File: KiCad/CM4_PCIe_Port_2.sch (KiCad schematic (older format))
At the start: 1 part, among them J14 10018783-10113TLF

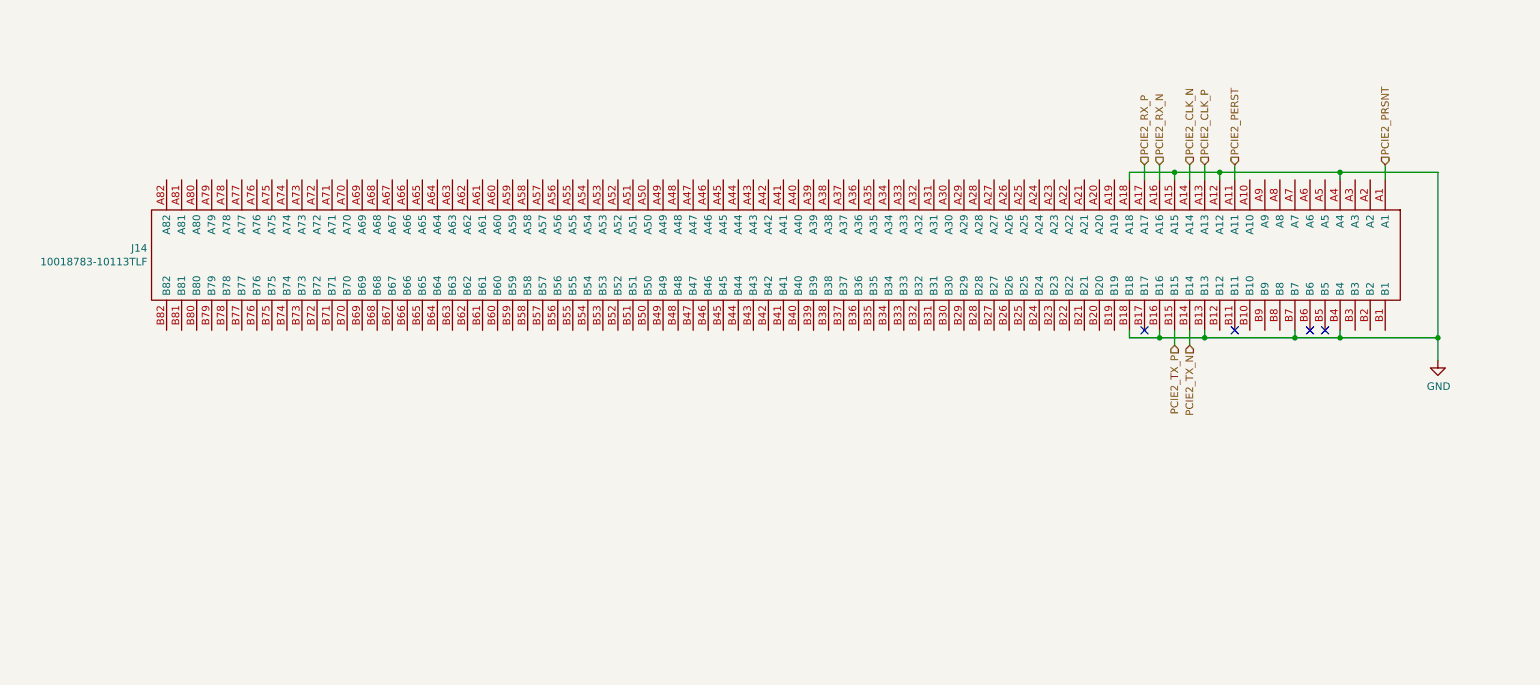
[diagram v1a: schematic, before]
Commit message: Updating PCIe symbols + PCIe power stub sheet
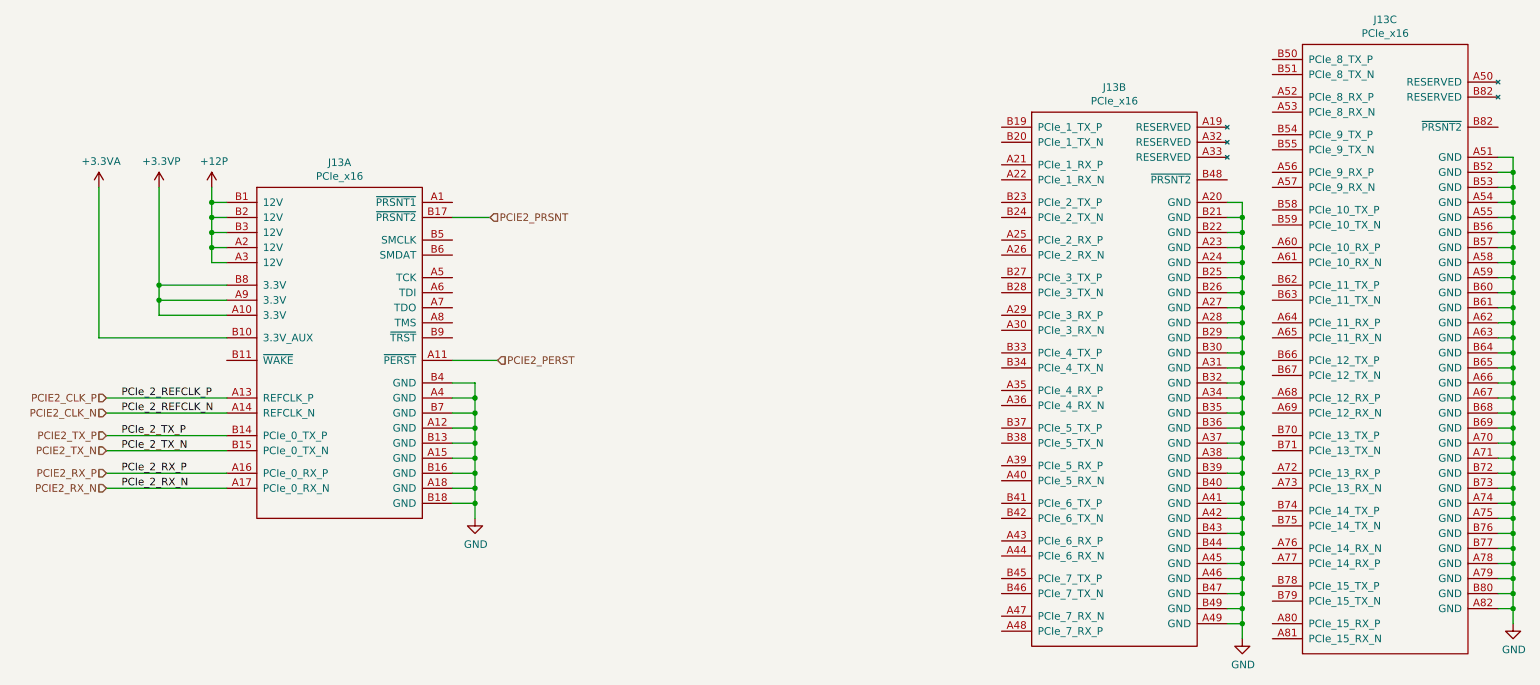
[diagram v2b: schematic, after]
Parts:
- removed J14: 10018783-10113TLF, CM4_MATX:10018783-10113TLF, symbol CM4_MATX:10018783-10113TLF
- added J13: PCIe_x16, CM4_MATX:10018783-10113TLF, symbol CM4_MATX:PCIe_x16
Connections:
- net GND: now also J13.A12 (GND), J13.A15 (GND), J13.A18 (GND), J13.A20 (GND), J13.A23 (GND), J13.A24 (GND), J13.A27 (GND), J13.A28 (GND), J13.A31 (GND), J13.A34 (GND), J13.A37 (GND), J13.A38 (GND), J13.A4 (GND), J13.A41 (GND), J13.A42 (GND), J13.A45 (GND), J13.A46 (GND), J13.A49 (GND), J13.A51 (GND), J13.A54 (GND), J13.A55 (GND), J13.A58 (GND), J13.A59 (GND), J13.A62 (GND), J13.A63 (GND), J13.A66 (GND), J13.A67 (GND), J13.A70 (GND), J13.A71 (GND), J13.A74 (GND), J13.A75 (GND), J13.A78 (GND), J13.A79 (GND), J13.A82 (GND), J13.B13 (GND), J13.B16 (GND), J13.B18 (GND), J13.B21 (GND), J13.B22 (GND), J13.B25 (GND), J13.B26 (GND), J13.B29 (GND), J13.B30 (GND), J13.B32 (GND), J13.B35 (GND), J13.B36 (GND), J13.B39 (GND), J13.B4 (GND), J13.B40 (GND), J13.B43 (GND), J13.B44 (GND), J13.B47 (GND), J13.B49 (GND), J13.B52 (GND), J13.B53 (GND), J13.B56 (GND), J13.B57 (GND), J13.B60 (GND), J13.B61 (GND), J13.B64 (GND), J13.B65 (GND), J13.B68 (GND), J13.B69 (GND), J13.B7 (GND), J13.B72 (GND), J13.B73 (GND), J13.B76 (GND), J13.B77 (GND), J13.B80 (GND)
- net PCIE2_CLK_N: now also J13.A14 (REFCLK_N)
- net PCIE2_CLK_P: now also J13.A13 (REFCLK_P)
- net PCIE2_PERST: now also J13.A11 (~PERST)
- net PCIE2_PRSNT: now also J13.B17 (~PRSNT2)
- net PCIE2_RX_N: now also J13.A17 (PCIe_0_RX_N)
- net PCIE2_RX_P: now also J13.A16 (PCIe_0_RX_P)
- net PCIE2_TX_N: now also J13.B15 (PCIe_0_TX_N)
- net PCIE2_TX_P: now also J13.B14 (PCIe_0_TX_P)
- new net +12P: J13.A2 (12V), J13.A3 (12V), J13.B1 (12V), J13.B2 (12V), J13.B3 (12V)
- new net +3.3VA: J13.B10 (3.3V_AUX)
- new net +3.3VP: J13.A10 (3.3V), J13.A9 (3.3V), J13.B8 (3.3V)
- no-connect marks 4 -> 0
